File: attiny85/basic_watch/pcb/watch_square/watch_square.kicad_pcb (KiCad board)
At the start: 2 copper layers, 39.9 x 41.8 mm, 22 parts, among them P1 JST_LIPO, U2 MCP73831-2-OT

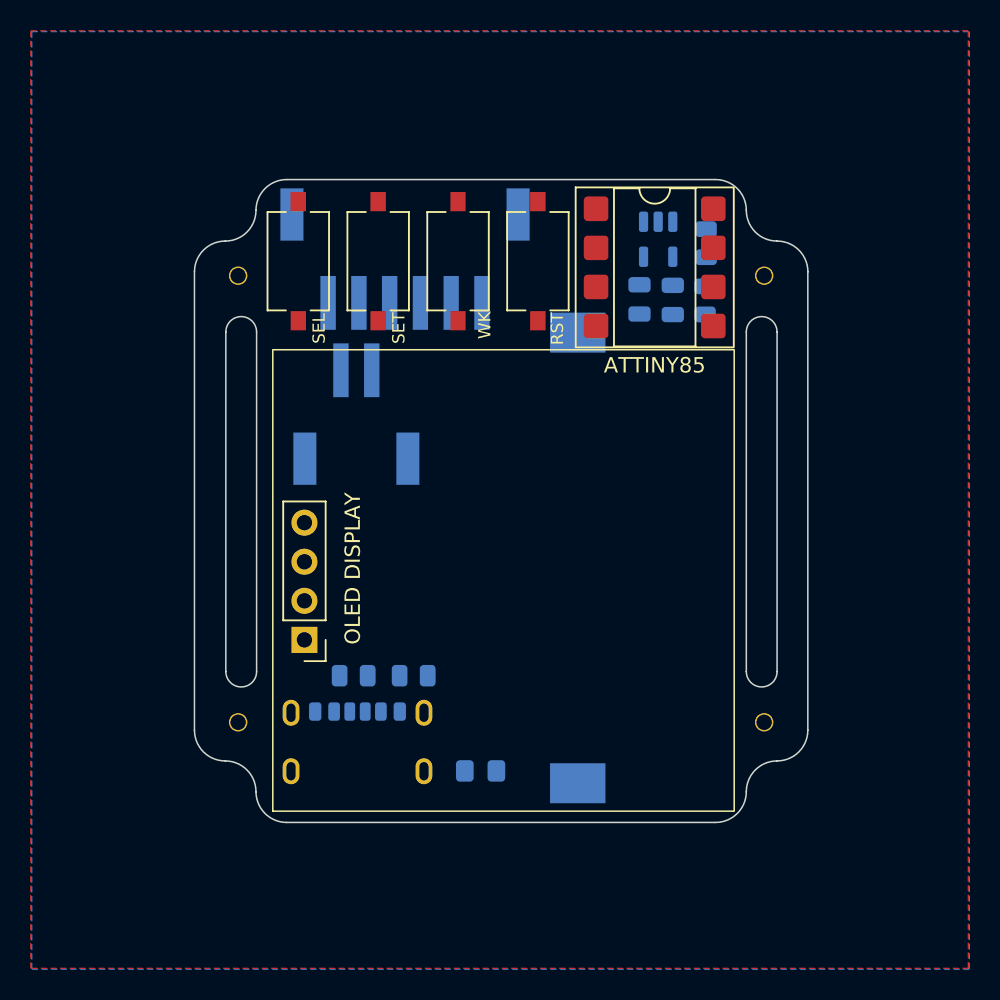
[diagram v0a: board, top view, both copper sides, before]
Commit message: Round watch footprint cannot accomodate all components
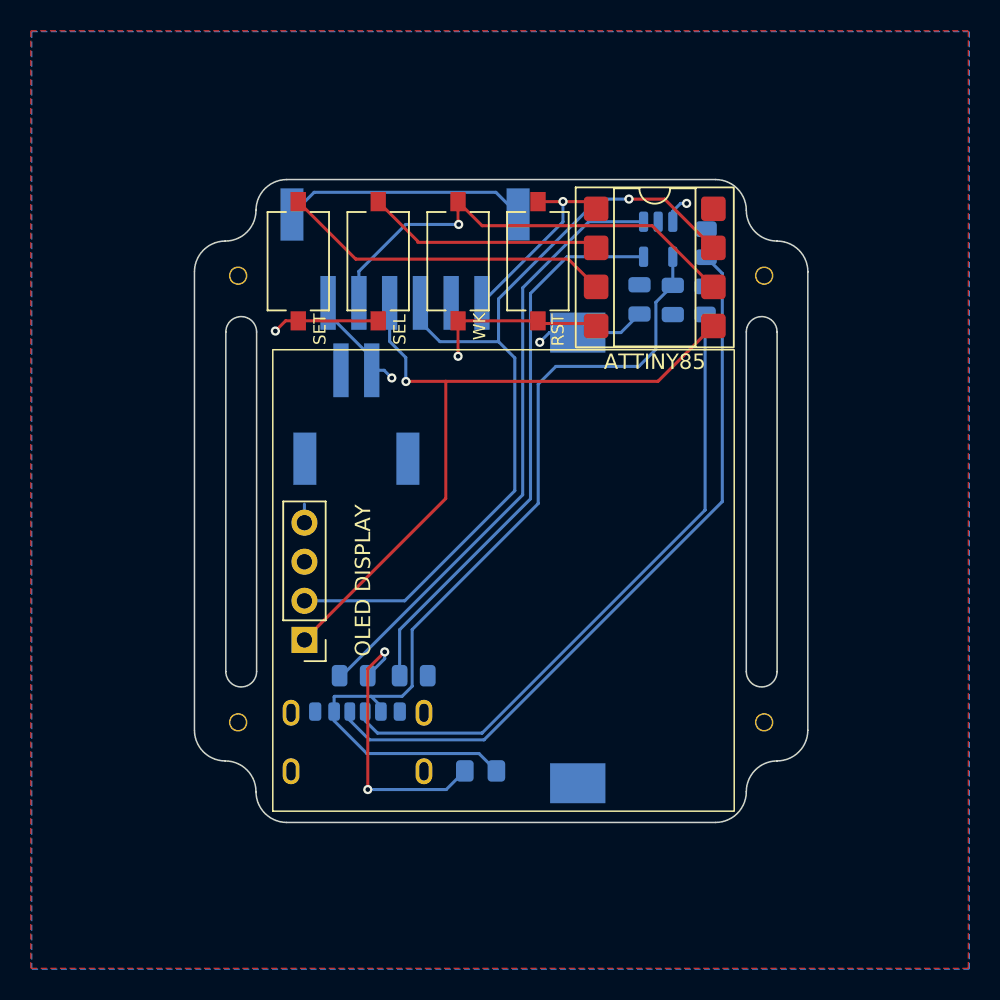
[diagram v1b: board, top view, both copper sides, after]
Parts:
- BT1: value Battery_Cell -> BT1
- J2: renamed from JPROG; value Programmer -> PROG
- OLED_DISPLAY1: renamed from OLED DISPLAY; value SSD1306_OLED_Display_128x64 -> OLED DISPLAY
- P1: value JST_LIPO -> LIPO B2
- R1: value 5.1k -> 6.8k
- R2: value 5.1k -> 470
- R3: value 6.8k -> 5.1k
- R4: value 470 -> 5.1k
- RST1: renamed from RST; value Reset -> RST
- SEL1: renamed from SEL; value Select -> SEL
- SET1: renamed from SET; value Set -> SET
- WK1: renamed from WK; value Wake -> WK
- moved SEL1 5.19 mm to (137.9, 70.9)
- moved SET1 5.19 mm to (132.7, 70.9)
- renumbered ATTINY85 to ATTINY1, USBC to J1, LED to LED1, U2 to U1
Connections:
- J1 pad A5: Net-(J2-CC1) -> Net-(J1-CC1)
- J1 pad B5: Net-(J2-CC2) -> Net-(J1-CC2)
- J2 pad S1: Net-(J3-SHIELD-PadS1) -> GND
- J2 pad S2: Net-(J3-SHIELD-PadS1) -> GND
- OLED_DISPLAY1 pad 1: GND -> MOSI
- OLED_DISPLAY1 pad 2: VCC -> SCK
- OLED_DISPLAY1 pad 3: SCK -> VCC
- OLED_DISPLAY1 pad 4: MOSI -> GND
- R1 pad 1: Net-(J2-CC1) -> GND
- R1 pad 2: GND -> Net-(U1-PROG)
- R2 pad 1: Net-(J2-CC2) -> Net-(LED1-K)
- R2 pad 2: GND -> Net-(U1-STAT)
- R3 pad 1: GND -> Net-(J1-CC1)
- R3 pad 2: Net-(U2-PROG) -> GND
- R4 pad 1: Net-(LED1-K) -> Net-(J1-CC2)
- R4 pad 2: Net-(U2-STAT) -> GND
- U1 pad 1: Net-(U2-STAT) -> Net-(U1-STAT)
- U1 pad 5: Net-(U2-PROG) -> Net-(U1-PROG)
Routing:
- net VBUS: track 0.00 -> 58.2 mm
- net SCK: track 0.00 -> 54.4 mm, vias 0 -> 1
- net Net-(J1-CC2): track 0.00 -> 48.1 mm
- net MOSI: track 0.00 -> 47.2 mm, vias 0 -> 1
- net Net-(J1-CC1): track 0.00 -> 41.8 mm
- net Net-(U1-STAT): track 0.00 -> 39.9 mm
- net Net-(U1-PROG): track 0.00 -> 36.7 mm
- net GND: track 0.00 -> 35.5 mm, vias 0 -> 2
- net MISO: track 0.00 -> 30.2 mm, vias 0 -> 1
- net SET: track 0.00 -> 22.1 mm
- net Net-(LED1-K): track 0.00 -> 18.2 mm, vias 0 -> 2
- net VCC: track 0.00 -> 17.1 mm, vias 0 -> 3
- net SELECT: track 0.00 -> 15.4 mm
- net RESET: track 0.00 -> 12.8 mm, vias 0 -> 1
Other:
- board text added: "Parten Ranch Robotics"

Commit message: changed footprints
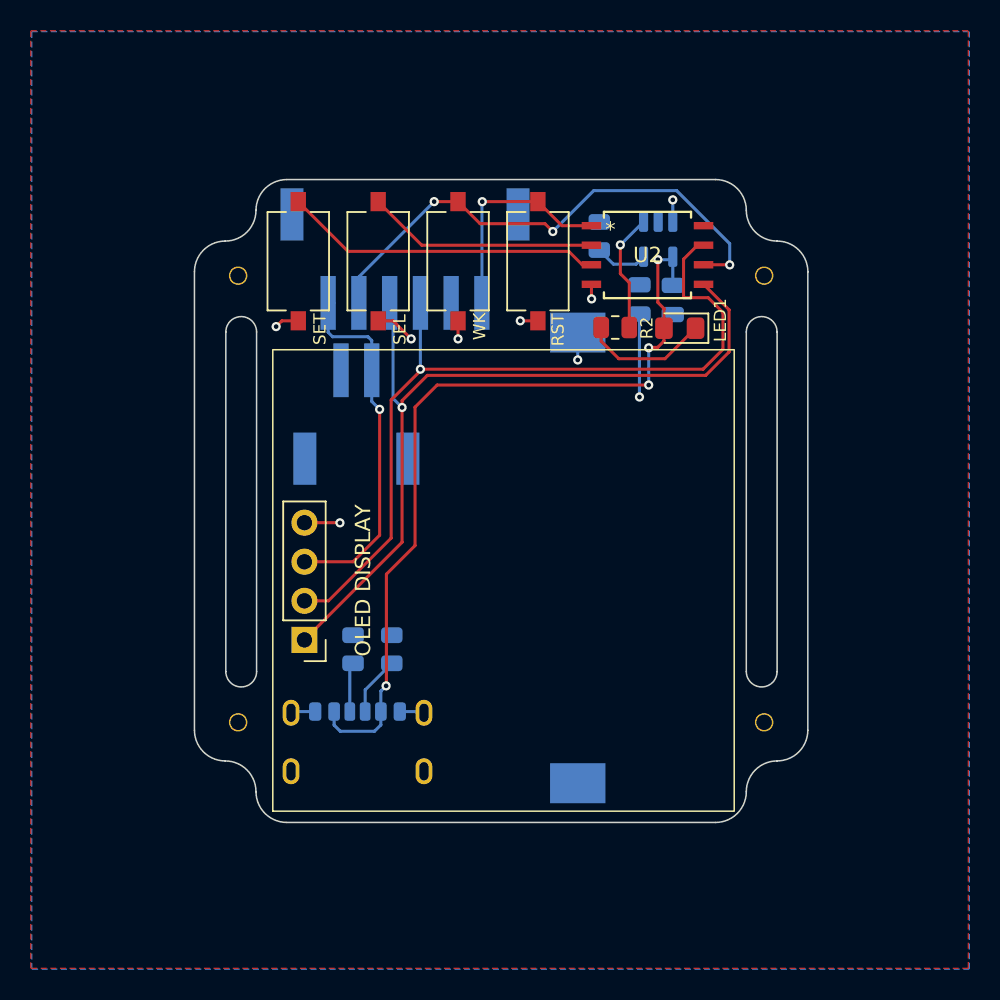
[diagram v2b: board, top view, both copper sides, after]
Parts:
- removed ATTINY1: ATTINY85, Package_DIP:DIP-8_W7.62mm_SMDSocket_SmallPads
- added U2: ATTINY85-20SUR, My_ATTINY:8S2_ATM-L, F.Cu at (155.4, 70.5)
- LED1, R2: moved to F.Cu
- moved R4 35.0 mm to (136.3, 96.1)
- moved LED1 31.6 mm to (157.5, 75.3), turned to 180 degrees
- moved R1 31.0 mm to (152.3, 69.3), turned to -90 degrees
- moved R3 30.5 mm to (138.8, 96.1)
- moved R2 28.3 mm to (153.3, 75.2), turned to 0 degrees
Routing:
- net Net-(J1-CC2): track 48.1 -> 3.23 mm
- net Net-(J1-CC1): track 41.8 -> 3.86 mm
- net Net-(U1-PROG): track 36.7 -> 3.46 mm
- net Net-(U1-STAT): track 39.9 -> 7.74 mm, vias 0 -> 1
- net GND: track 35.5 -> 12.6 mm, vias 2 -> 6
- net VCC: track 17.1 -> 32.5 mm, vias 3 -> 4
- net Net-(LED1-K): track 18.2 -> 8.31 mm, vias 2 -> 0
- net MOSI: track 47.2 -> 53.0 mm
- net MISO: track 30.2 -> 34.5 mm, vias 1 -> 3
- net VBUS: track 58.2 -> 54.2 mm, vias 0 -> 4
- net RESET: track 12.8 -> 14.3 mm
- net SET: track 22.1 -> 20.8 mm
- net SCK: track 54.4 -> 53.5 mm

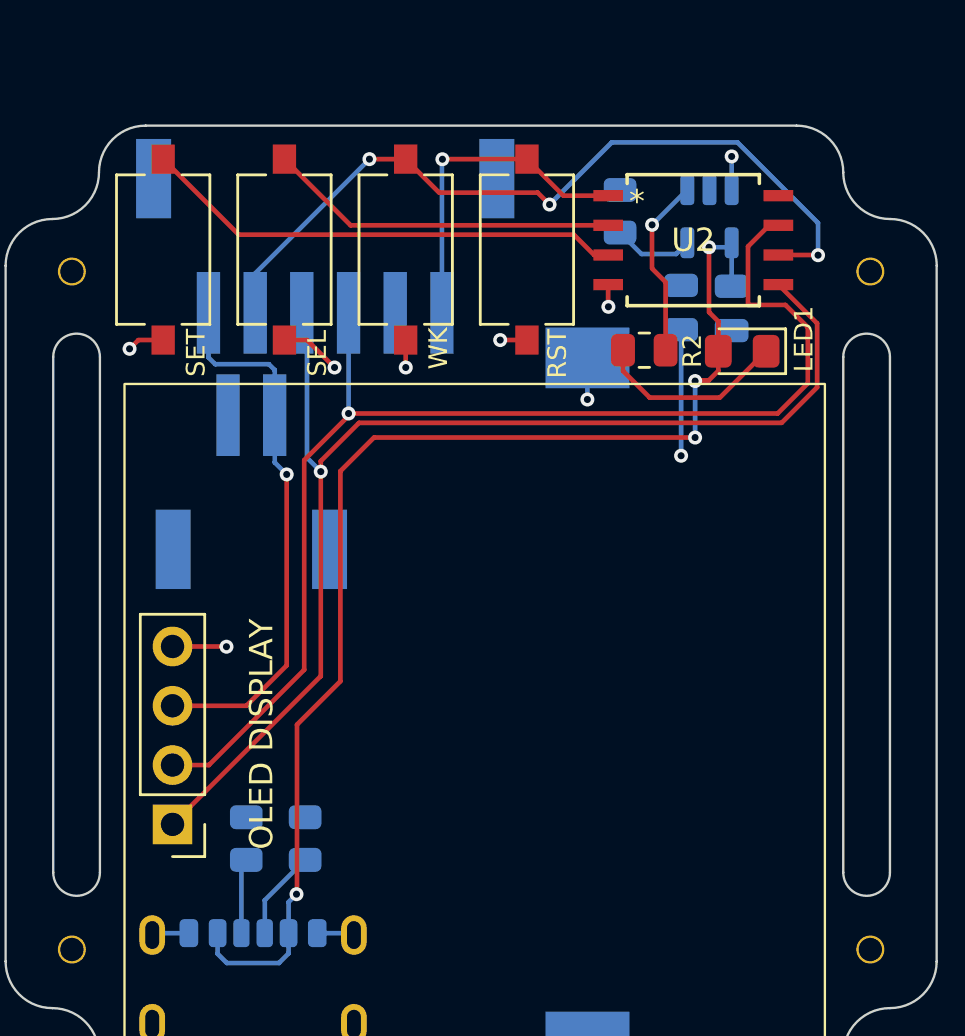
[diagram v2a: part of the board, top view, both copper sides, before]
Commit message: corrected OLED orientation
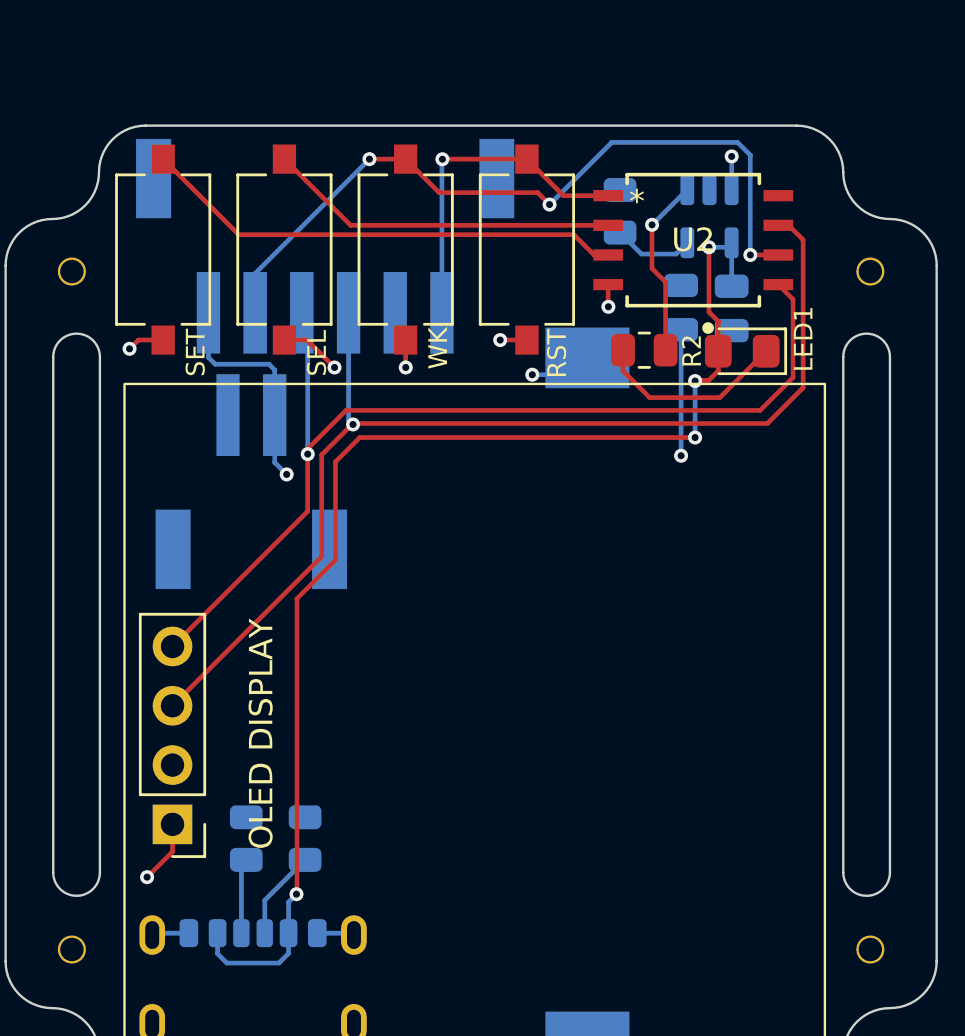
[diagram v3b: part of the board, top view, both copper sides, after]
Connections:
- OLED_DISPLAY1 pad 1: MOSI -> GND
- OLED_DISPLAY1 pad 2: SCK -> VCC
- OLED_DISPLAY1 pad 3: VCC -> SCK
- OLED_DISPLAY1 pad 4: GND -> MOSI
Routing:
- net VCC: track 32.5 -> 19.6 mm
- net MOSI: track 53.0 -> 43.6 mm
- net SCK: track 53.5 -> 48.1 mm
- net MISO: track 34.5 -> 32.8 mm
- net GND: track 12.6 -> 13.3 mm
